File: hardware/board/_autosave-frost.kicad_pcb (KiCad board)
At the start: 2 copper layers, 90 x 55 mm, 565 parts, among them CN1 PJ-393 8PJ, CN2 1-2199230-5, CN2 35RAPC4BH3, J1 HDMI_A, Q1 WPM3407-3/TR, Q2 SS8050, Q3 WPM2015-3/TR_C7472861, Q4 WPM2015-3/TR_C7472861, Q5 SS8050, Q6 2SK3018_C194460, Q7 2SK3018_C194460, Q8 2SK3018_C194460, U1 RK3568, U10 SY8088AAC, U11 RK860-0, U12 SY7208ABC, U13 FTC252012SR24MBCA, U14 ESD5311X, U15 ESD5311X, U16 ESD5311X, U17 ESD5311X, U18 SY6280AAC, U19 ESD5311X, U2 K4UCE3Q4AB-MGCL, U20 ESD5311X, U21 ESD5311X, U22 ESD5311X, U23 ESD5311X, U24 ESD5311X, U25 ESD5311X, U26 LP3983SAB5F-08, U27 5054133410_C6422029, U28 ESD5341N, U29 ESD5341N, U3 KLMBG2JETD-B041_C5821038, U30 ESD5341N, U31 ESD5341N, U32 SY7203DBC, U33 CY54-4.7UH, U34 AP6275PR3, U35 TFM252012ALVA2R2MTAA, U36 RTL8211F-CG, U37 TFM252012ALVA2R2MTAA, U38 ESD5451N_C5261080, U39 ESD5451N_C5261080, U4 RK809-5, U40 ESD5451N_C5261080, U41 ESD5451N_C5261080, U42 ESD5451N_C5261080, U43 ESD5451N_C5261080, U44 ESD5451N_C5261080, U45 ESD5451N_C5261080, U46 ESD5451N_C5261080, U47 ESD5451N_C5261080, U48 ESD5451N_C5261080, U49 ESD5451N_C5261080, U5 TFM252012ALVA2R2MTAA, U6 TMUXHS4212RKSR, U7 FUSB302BMPX, U8 BQ25890RTWR, U9 S2B-PH-K-S(LF)(SN), X1 24 MHz, X2 Q13FC1350000400, X3 S3237400121040, X4 X322525MOB4SI

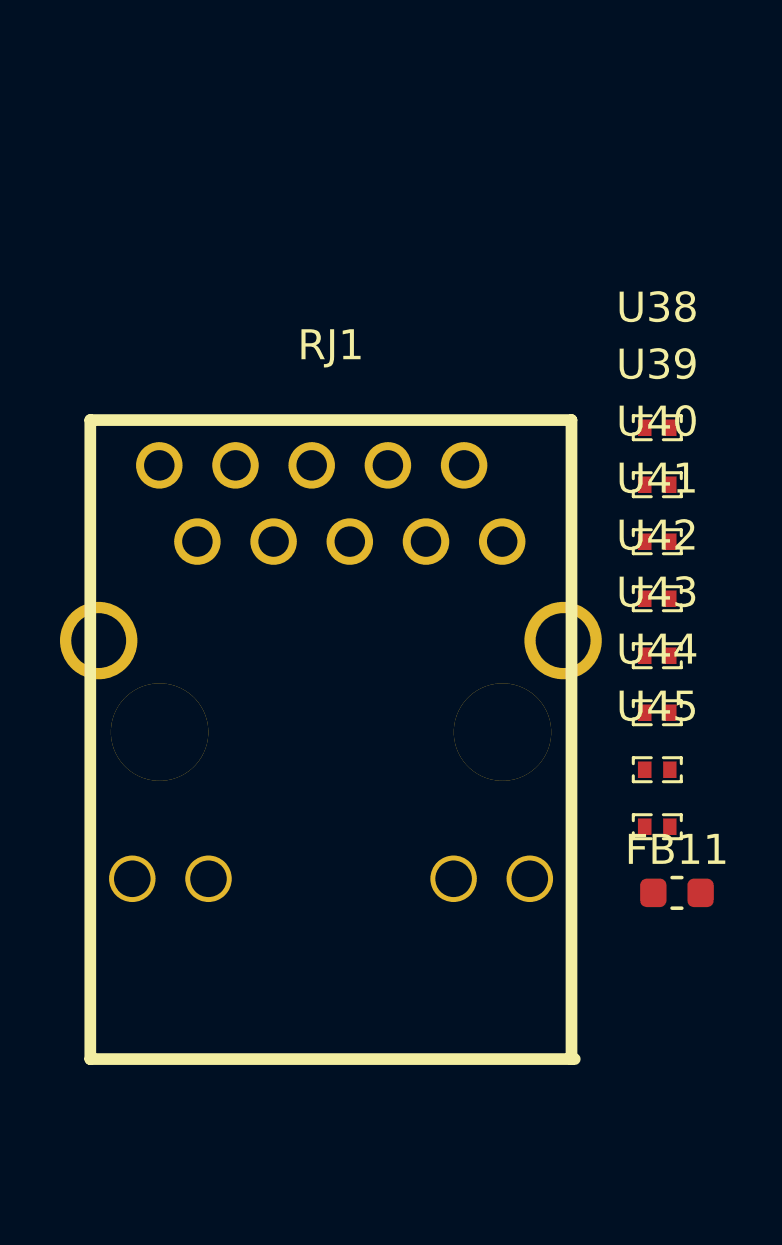
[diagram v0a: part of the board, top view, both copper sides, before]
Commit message: add in pcie and ddr4
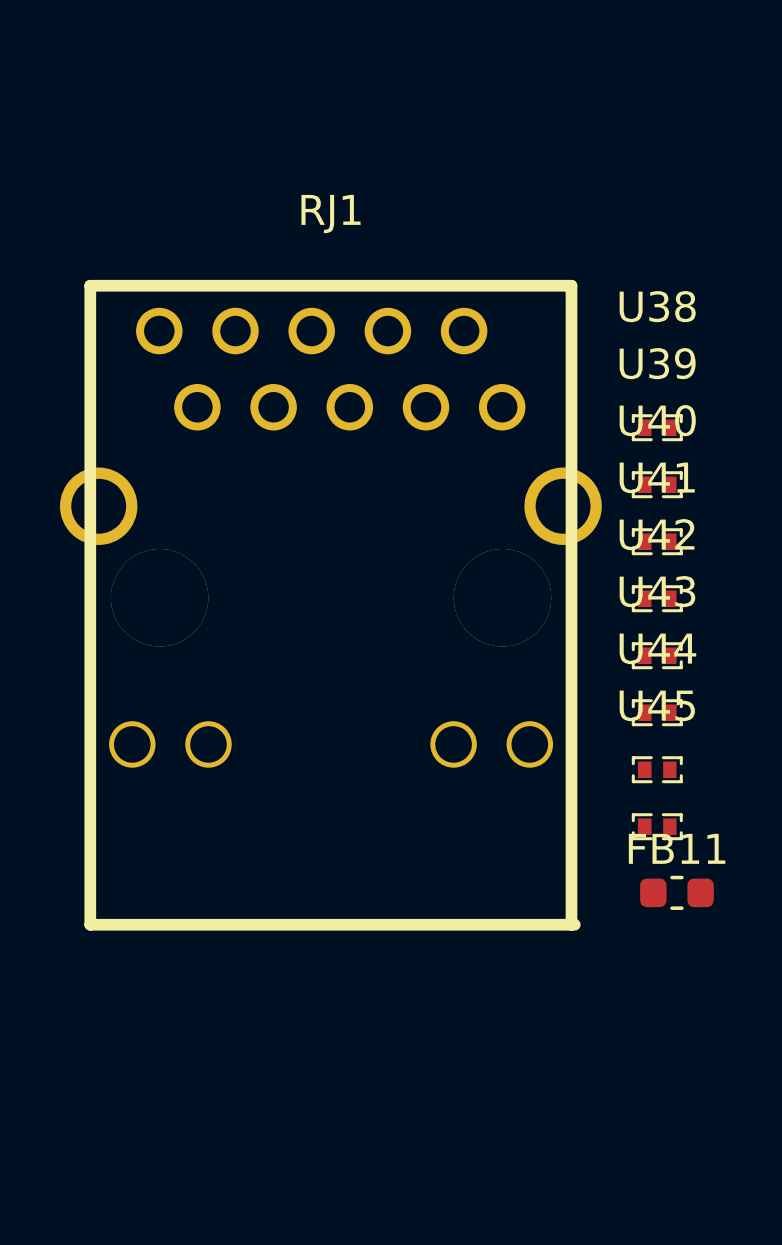
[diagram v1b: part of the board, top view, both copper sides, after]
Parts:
- moved RJ1 4.48 mm to (25.8, 116.8)
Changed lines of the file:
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@@
 	(footprint "lcsc:RJ45-TH_10P-P2.54-S2.54_L16.1-W21.4_HY911130A"
 		(layer "F.Cu")
-		(at 25.7775 121.2275)
+		(at 25.7775 116.75)
 		(property "Reference" "RJ1"
 			(at 0 -10.89 0)
